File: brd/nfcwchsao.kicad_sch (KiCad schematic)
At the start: 12 parts, among them J1 Conn_02x03_Odd_Even, U1 NT3H2211, U2 CH32V003F4P6

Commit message: updating part numbers and documenation
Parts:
- D1: MPN (none) -> QLS6A-FKW-CNSNSF043
- LS1: MPN (none) -> PKLCS1212E20A0-R1
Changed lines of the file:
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@@
+      (effects (font (size 1.27 1.27)) hide)
+    )
+    (property "MPN" "PKLCS1212E20A0-R1" (at 105.41 95.25 0)
       (effects (font (size 1.27 1.27)) hide)
     )
@@
       (effects (font (size 1.27 1.27)) hide)
     )
+    (property "MPN" "QLS6A-FKW-CNSNSF043" (at 190.5 63.5 0)
+      (effects (font (size 1.27 1.27)) hide)
+    )

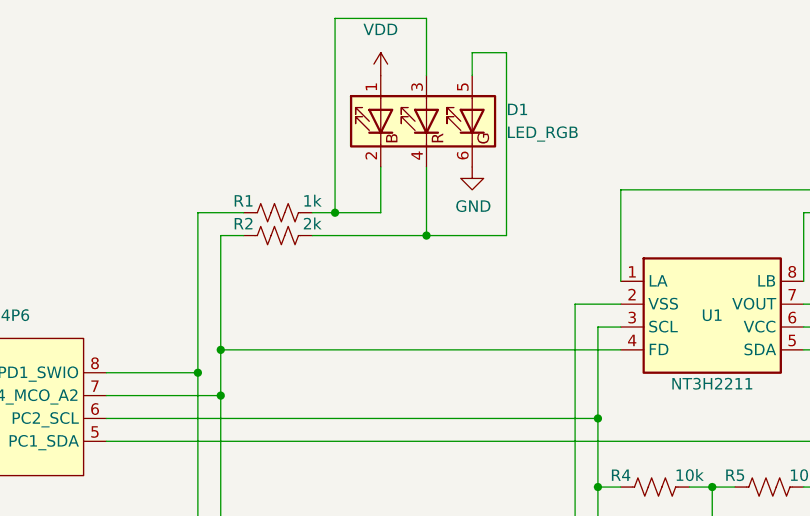
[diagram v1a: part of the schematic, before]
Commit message: updating to hand solder buzzer footprint, staggered header, single color LED
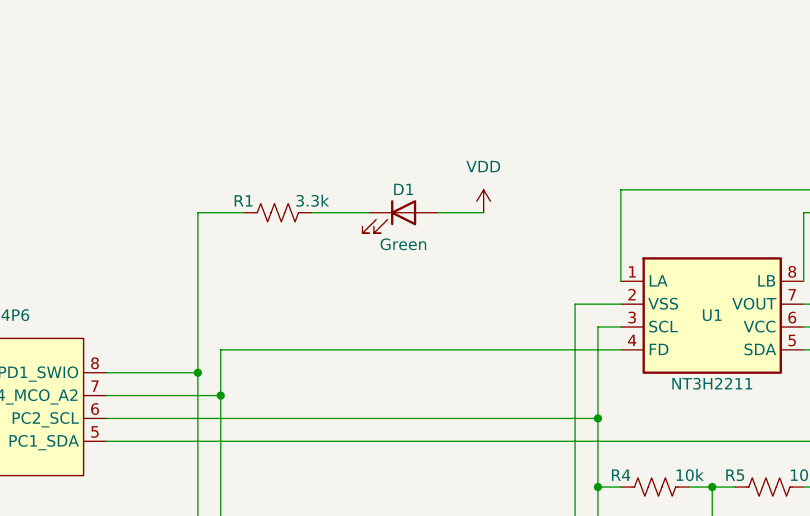
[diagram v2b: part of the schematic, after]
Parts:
- removed D1: LED_RGB, custom:LED_Cree-PLCC6_4.7x1.5mm_extended pads, symbol custom:LED_BRG
- removed R2: 2k, Resistor_SMD:R_0603_1608Metric_Pad0.98x0.95mm_HandSolder, symbol Device:R_US
- added D1: Green, custom:LED_Right_Angle_3x2x1mm, symbol Device:LED
- J1: footprint Connector_PinHeader_2.54mm:PinHeader_2x03_P2.54mm_Vertical -> custom:PinHeader_2x03_P2.54mm_Staggered
- LS1: footprint Buzzer_Beeper:Buzzer_Murata_PKLCS1212E -> custom:Buzzer_Murata_PKLCS1212E_handy
- R1: value 1k -> 3.3k
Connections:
- net VDD: now also D1.2 (A)
- net at R1.1: now also D1.1 (K)

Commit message: cleaned up BOM, changed KiCad logo to all silkscreen
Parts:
- C1: value 1uF -> 4.7uF; LCSC C14445 -> C1705; MPN CL05A105KP5NNNC -> CL10A475KP8NNNC
- C2, GS1, J1: now not fitted
- D1: LCSC (none) -> C7202185; MPN (none) -> HSMG-C110
- LS1: LCSC (none) -> C3811858
- R1: LCSC (none) -> C108078; MPN (none) -> RC0603FR-073K3L
- R4, R5: LCSC (none) -> C98220; MPN (none) -> RC0603FR-0710KL
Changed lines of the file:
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@@
 			)
 		)
-		(property "Value" "1uF"
+		(property "Value" "4.7uF"
 			(at 142.0368 117.983 0)
 			(effects
@@
 			)
 		)
-		(property "LCSC" "C14445"
+		(property "LCSC" " C1705"
 			(at 139.7 116.84 0)
 			(effects
@@
 			)
 		)
-		(property "MPN" "CL05A105KP5NNNC"
+		(property "MPN" "CL10A475KP8NNNC"
 			(at 139.7 116.84 0)
 			(effects
@@
 		(in_bom yes)
 		(on_board yes)
-		(dnp no)
+		(dnp yes)
 		(property "Reference" "C2"
 			(at 249.9868 71.2216 0)
@@
 		(in_bom yes)
 		(on_board yes)
-		(dnp no)
+		(dnp yes)
 		(property "Reference" "GS1"
 			(at 189.23 179.07 0)
@@
 		)
 		(property "Description" "Light emitting diode"
+			(at 187.96 73.66 0)
+			(effects
+				(font
+					(size 1.27 1.27)
+				)
+				(hide yes)
+			)
+		)
+		(property "LCSC" "C7202185"
+			(at 187.96 73.66 0)
+			(effects
+				(font
+					(size 1.27 1.27)
+				)
+				(hide yes)
+			)
+		)
+		(property "MPN" "HSMG-C110"
 			(at 187.96 73.66 0)
 			(effects
@@
 			)
 		)
+		(property "LCSC" "C3811858"
+			(at 105.41 95.25 0)
+			(effects
+				(font
+					(size 1.27 1.27)
+				)
+				(hide yes)
+			)
+		)
 		(pin "1"
 		)
@@
 			)
 		)
-		(property "LCSC" ""
+		(property "LCSC" "C98220"
 			(at 228.6 104.14 0)
 			(effects
@@
 			)
 		)
-		(property "MPN" ""
+		(property "MPN" "RC0603FR-0710KL"
 			(at 228.6 104.14 0)
 			(effects
@@
 			)
 		)
-		(property "LCSC" ""
+		(property "LCSC" "C108078"
 			(at 173.99 73.66 0)
 			(effects
@@
 			)
 		)
-		(property "MPN" ""
+		(property "MPN" "RC0603FR-073K3L"
 			(at 173.99 73.66 0)
 			(effects
@@
 			)
 		)
-		(property "LCSC" ""
+		(property "LCSC" "C98220"
 			(at 215.9 104.14 0)
 			(effects
@@
 			)
 		)
-		(property "MPN" ""
+		(property "MPN" "RC0603FR-0710KL"
 			(at 215.9 104.14 0)
 			(effects
@@
 		(in_bom yes)
 		(on_board yes)
-		(dnp no)
+		(dnp yes)
 		(property "Reference" "J1"
 			(at 222.25 110.49 0)
